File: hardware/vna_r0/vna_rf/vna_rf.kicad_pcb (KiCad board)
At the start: 4 copper layers, 78 x 49 mm, 131 parts, among them J301 RF_Shield_Two_Pieces, J302 RF_Shield_Two_Pieces, J401 CONN_02X10, J402 RF_Shield_Two_Pieces, U201 LMX2594, U202 LTC2630, U203 ADRF5040, U204 LTC2054CS5, U205 MAAM-011100, U301 NC7WZU04, U302 PE42521, U303 MASW-008322-TR1000, U304 PE42521, U401 CONN_SMA_2GND, U402 CONN_SMA_2GND, U403 CONN_SMA, U404 CONN_SMA, U405 CONN_SMA, U406 CONN_SMA_2GND

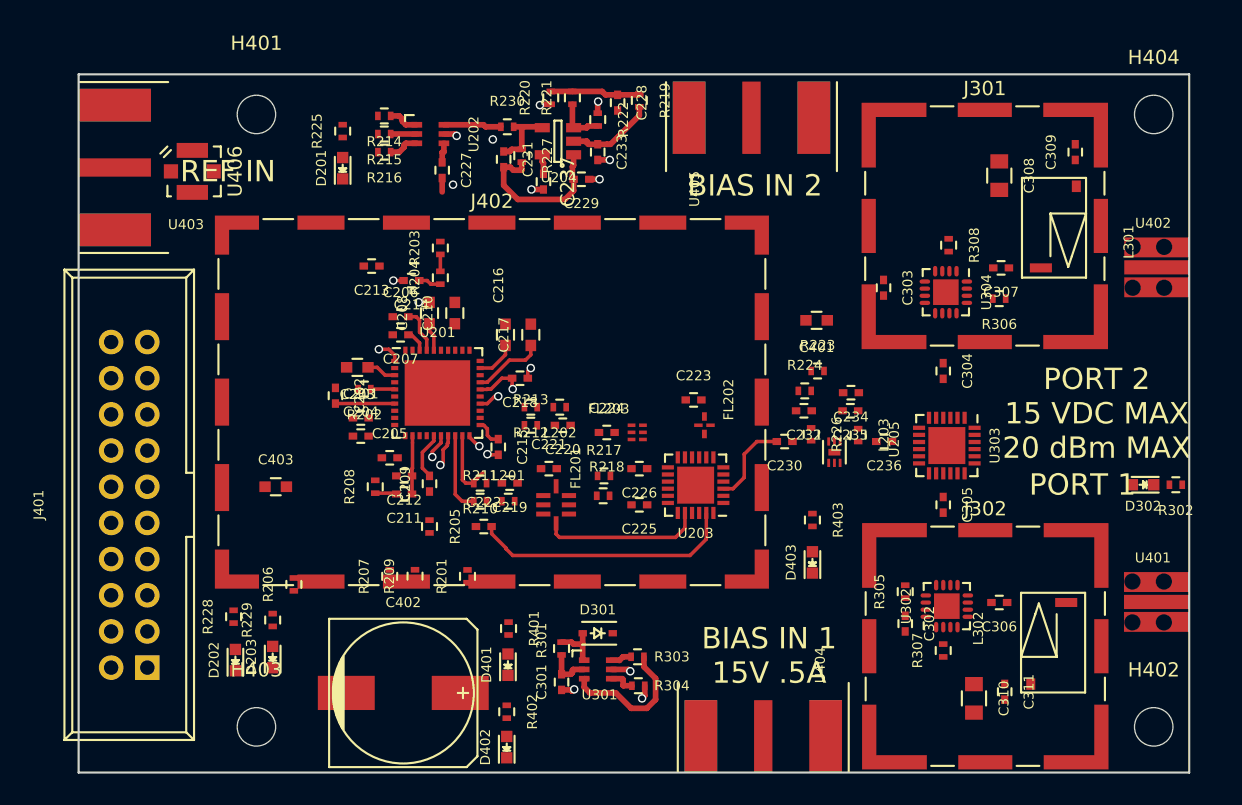
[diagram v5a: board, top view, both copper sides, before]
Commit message: routing vna rf r0
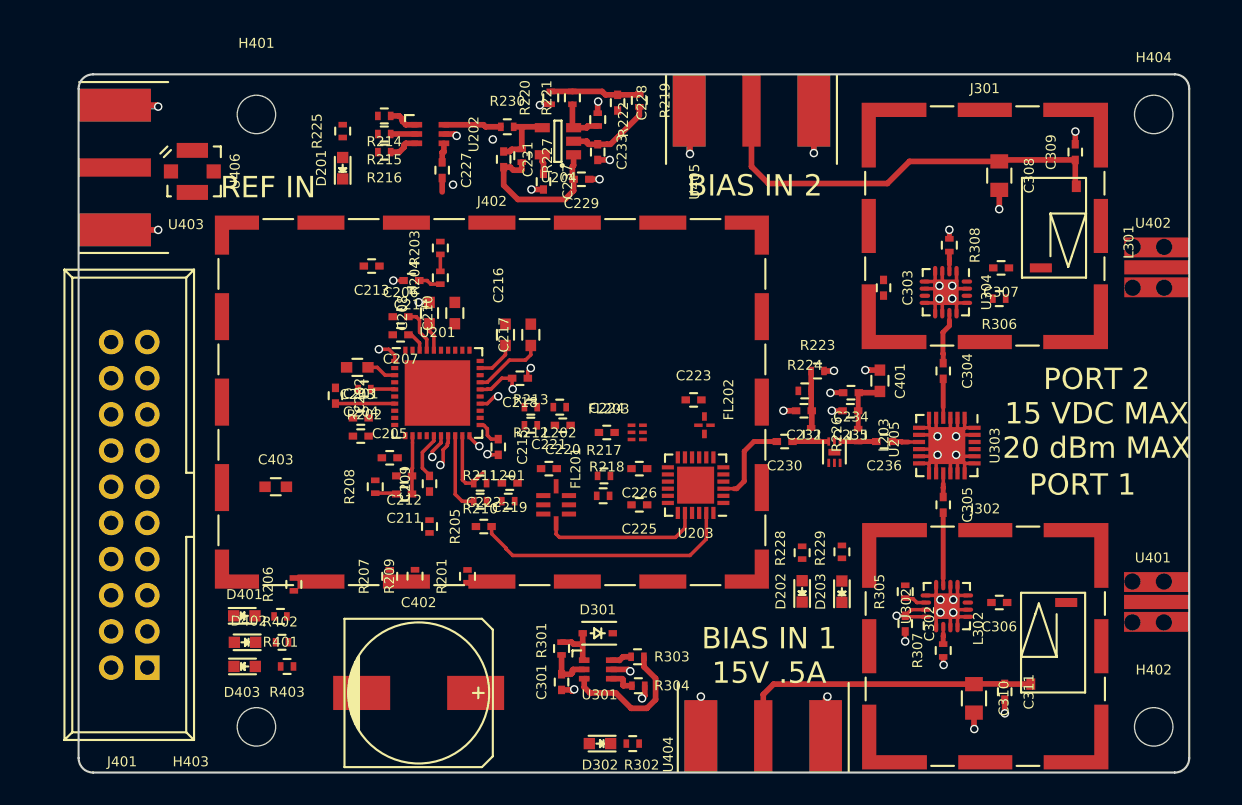
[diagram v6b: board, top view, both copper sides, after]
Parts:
- moved R302 42.2 mm to (214.4, 122.2)
- moved D302 42.2 mm to (212.1, 122.2)
- moved D403 40.5 mm to (187.2, 116.8), turned to 0 degrees
- moved R229 40.3 mm to (229.1, 108.7)
- moved D203 40.2 mm to (229.1, 111.5)
- moved R228 40.2 mm to (226.3, 108.8)
- moved D202 40.1 mm to (226.3, 111.5)
- moved R403 38.3 mm to (190.2, 116.8), turned to 180 degrees
- moved D402 19.8 mm to (187.2, 115.1), turned to 180 degrees
- moved D401 18.8 mm to (187.2, 113.2), turned to 0 degrees
- moved R402 16.5 mm to (189.8, 115.1), turned to 0 degrees
- moved R401 16.0 mm to (189.7, 113.2), turned to 180 degrees
- moved C401 6.15 mm to (231.8, 96.7), turned to 90 degrees
- moved C402 1.08 mm to (199.4, 118.6)
- moved U405 0.51 mm to (222.8, 77.7)
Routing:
- net GND: track 11.4 -> 102.5 mm, vias 12 -> 42
- net /PORT2_BIAS: track 0.00 -> 29.2 mm
- net /PORT1_BIAS: track 0.00 -> 22.0 mm
- net Net-(C305-Pad2): track 0.00 -> 5.09 mm
- net /AMP_5V: track 0.00 -> 4.06 mm
- net Net-(C232-Pad1): track 0.00 -> 4.03 mm
- net Net-(C304-Pad1): track 0.00 -> 3.88 mm
- net +3V3: track 18.8 -> 22.5 mm, vias 1 -> 2
- net Net-(C236-Pad2): track 0.00 -> 2.76 mm
- net Net-(C304-Pad2): track 0.00 -> 2.74 mm
- net Net-(C230-Pad1): track 0.00 -> 2.55 mm
- net /port_switch/RFIN: track 0.00 -> 1.92 mm
- net Net-(C305-Pad1): track 0.00 -> 1.66 mm
- net Net-(R305-Pad1): track 0.00 -> 1.58 mm
- net Net-(R308-Pad2): track 0.00 -> 1.38 mm
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- added copper zone on In2.Cu, net +3V3
- added copper zone on In1.Cu, net GND
- added copper zone on In2.Cu, net GND
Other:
- outline, holes or cut-outs redrawn

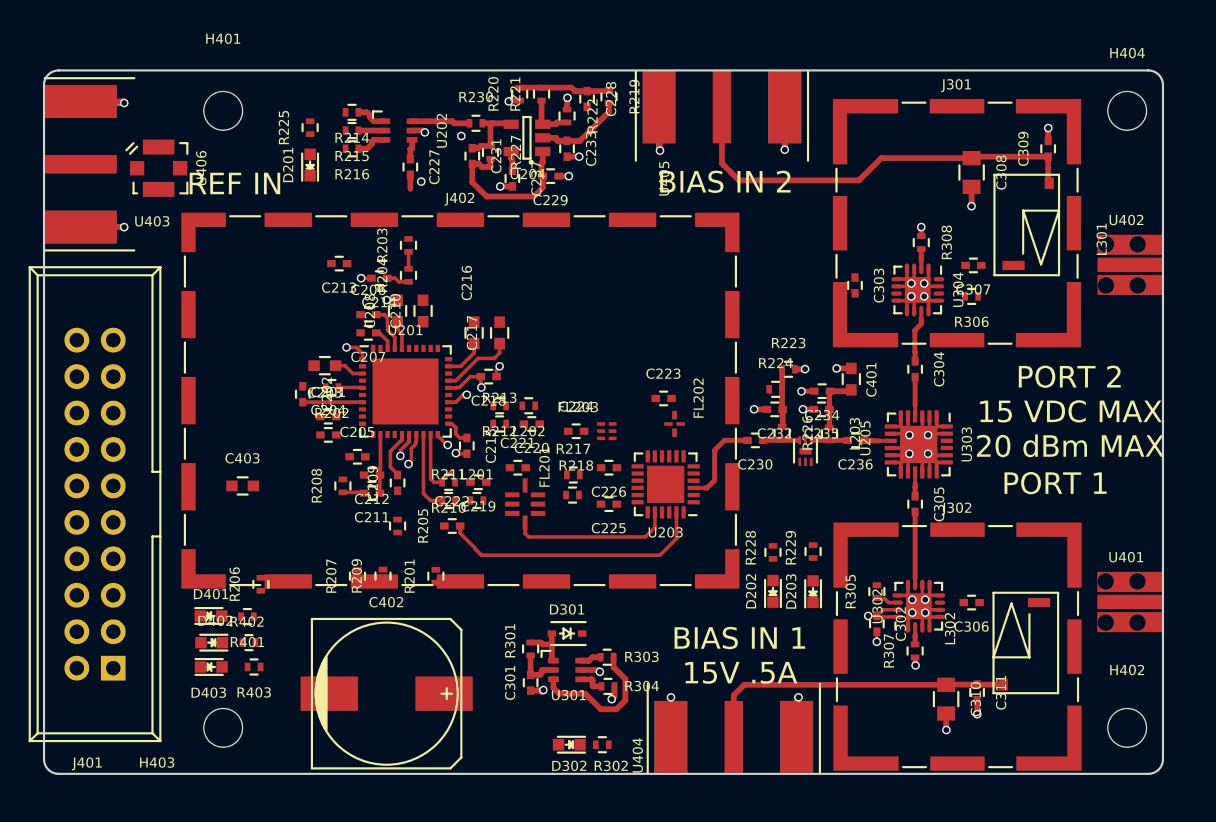
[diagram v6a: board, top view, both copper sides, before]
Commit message: layout of vna r0 rf board
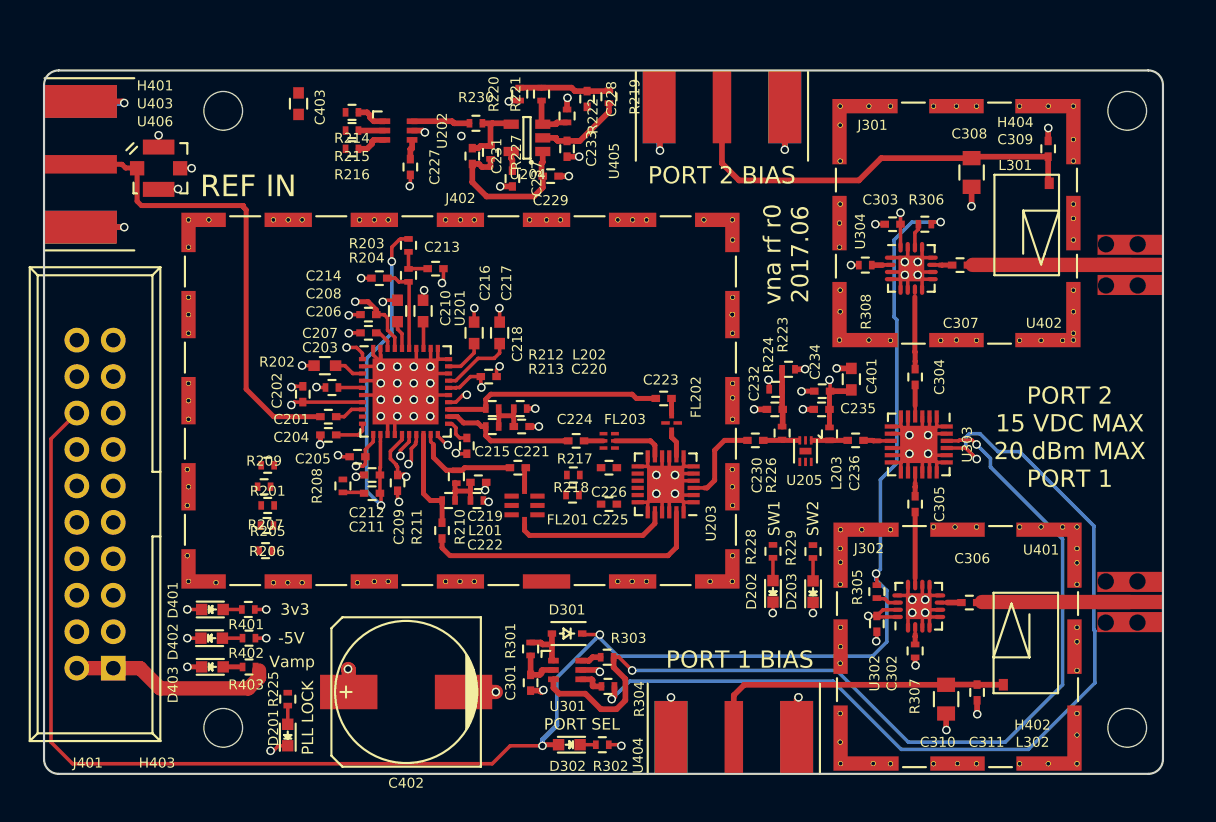
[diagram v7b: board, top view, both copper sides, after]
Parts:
- added REF**: VIA_OSH4LAYER_MIN, vna_footprints:VIA_OSH4LAYER_MIN, F.Cu at (223.5, 105.5)
- added REF** (x2): VIA_OSH4LAYER_MIN, vna_footprints:VIA_OSH4LAYER_MIN, F.Cu at (223.5, 92.2)
- added REF**: VIA_OSH4LAYER_MIN, vna_footprints:VIA_OSH4LAYER_MIN, F.Cu at (233.0, 77.7)
- added REF**: VIA_OSH4LAYER_MIN, vna_footprints:VIA_OSH4LAYER_MIN, F.Cu at (234.5, 77.7)
- added REF**: VIA_OSH4LAYER_MIN, vna_footprints:VIA_OSH4LAYER_MIN, F.Cu at (237.5, 77.7)
- added REF**: VIA_OSH4LAYER_MIN, vna_footprints:VIA_OSH4LAYER_MIN, F.Cu at (239.1, 77.7)
- added REF**: VIA_OSH4LAYER_MIN, vna_footprints:VIA_OSH4LAYER_MIN, F.Cu at (240.5, 77.7)
- added REF**: VIA_OSH4LAYER_MIN, vna_footprints:VIA_OSH4LAYER_MIN, F.Cu at (243.5, 77.7)
- added REF**: VIA_OSH4LAYER_MIN, vna_footprints:VIA_OSH4LAYER_MIN, F.Cu at (245.5, 77.7)
- added REF**: VIA_OSH4LAYER_MIN, vna_footprints:VIA_OSH4LAYER_MIN, F.Cu at (247.2, 77.7)
- added REF**: VIA_OSH4LAYER_MIN, vna_footprints:VIA_OSH4LAYER_MIN, F.Cu at (247.2, 80.0)
- added REF**: VIA_OSH4LAYER_MIN, vna_footprints:VIA_OSH4LAYER_MIN, F.Cu at (247.2, 81.5)
- added REF**: VIA_OSH4LAYER_MIN, vna_footprints:VIA_OSH4LAYER_MIN, F.Cu at (223.5, 87.0)
- added REF**: VIA_OSH4LAYER_MIN, vna_footprints:VIA_OSH4LAYER_MIN, F.Cu at (247.2, 84.5)
- added REF**: VIA_OSH4LAYER_MIN, vna_footprints:VIA_OSH4LAYER_MIN, F.Cu at (247.2, 85.5)
- added REF**: VIA_OSH4LAYER_MIN, vna_footprints:VIA_OSH4LAYER_MIN, F.Cu at (247.2, 87.0)
- added REF**: VIA_OSH4LAYER_MIN, vna_footprints:VIA_OSH4LAYER_MIN, F.Cu at (247.2, 90.5)
- added REF**: VIA_OSH4LAYER_MIN, vna_footprints:VIA_OSH4LAYER_MIN, F.Cu at (247.2, 92.0)
- added REF**: VIA_OSH4LAYER_MIN, vna_footprints:VIA_OSH4LAYER_MIN, F.Cu at (247.2, 93.5)
- added REF**: VIA_OSH4LAYER_MIN, vna_footprints:VIA_OSH4LAYER_MIN, F.Cu at (247.2, 94.0)
- added REF**: VIA_OSH4LAYER_MIN, vna_footprints:VIA_OSH4LAYER_MIN, F.Cu at (246.5, 94.0)
- added REF**: VIA_OSH4LAYER_MIN, vna_footprints:VIA_OSH4LAYER_MIN, F.Cu at (245.0, 94.0)
- added REF**: VIA_OSH4LAYER_MIN, vna_footprints:VIA_OSH4LAYER_MIN, F.Cu at (243.5, 94.0)
- added REF**: VIA_OSH4LAYER_MIN, vna_footprints:VIA_OSH4LAYER_MIN, F.Cu at (223.5, 85.6)
- added REF**: VIA_OSH4LAYER_MIN, vna_footprints:VIA_OSH4LAYER_MIN, F.Cu at (240.5, 94.0)
- added REF**: VIA_OSH4LAYER_MIN, vna_footprints:VIA_OSH4LAYER_MIN, F.Cu at (239.1, 94.0)
- added REF**: VIA_OSH4LAYER_MIN, vna_footprints:VIA_OSH4LAYER_MIN, F.Cu at (238.0, 94.0)
- added REF**: VIA_OSH4LAYER_MIN, vna_footprints:VIA_OSH4LAYER_MIN, F.Cu at (234.5, 94.0)
- added REF**: VIA_OSH4LAYER_MIN, vna_footprints:VIA_OSH4LAYER_MIN, F.Cu at (233.0, 94.0)
- added REF**: VIA_OSH4LAYER_MIN, vna_footprints:VIA_OSH4LAYER_MIN, F.Cu at (230.9, 94.0)
- added REF**: VIA_OSH4LAYER_MIN, vna_footprints:VIA_OSH4LAYER_MIN, F.Cu at (231.0, 92.0)
- added REF**: VIA_OSH4LAYER_MIN, vna_footprints:VIA_OSH4LAYER_MIN, F.Cu at (231.0, 90.5)
- added REF**: VIA_OSH4LAYER_MIN, vna_footprints:VIA_OSH4LAYER_MIN, F.Cu at (221.5, 85.6)
- added REF**: VIA_OSH4LAYER_MIN, vna_footprints:VIA_OSH4LAYER_MIN, F.Cu at (217.5, 85.6)
- added REF**: VIA_OSH4LAYER_MIN, vna_footprints:VIA_OSH4LAYER_MIN, F.Cu at (215.5, 85.6)
- added REF**: VIA_OSH4LAYER_MIN, vna_footprints:VIA_OSH4LAYER_MIN, F.Cu at (216.5, 85.6)
- added REF**: VIA_OSH4LAYER_MIN, vna_footprints:VIA_OSH4LAYER_MIN, F.Cu at (211.5, 85.6)
- added REF**: VIA_OSH4LAYER_MIN, vna_footprints:VIA_OSH4LAYER_MIN, F.Cu at (209.3, 85.6)
- added REF**: VIA_OSH4LAYER_MIN, vna_footprints:VIA_OSH4LAYER_MIN, F.Cu at (210.5, 85.6)
- added REF**: VIA_OSH4LAYER_MIN, vna_footprints:VIA_OSH4LAYER_MIN, F.Cu at (223.5, 103.0)
- added REF**: VIA_OSH4LAYER_MIN, vna_footprints:VIA_OSH4LAYER_MIN, F.Cu at (205.5, 85.6)
- added REF**: VIA_OSH4LAYER_MIN, vna_footprints:VIA_OSH4LAYER_MIN, F.Cu at (203.5, 85.6)
- added REF**: VIA_OSH4LAYER_MIN, vna_footprints:VIA_OSH4LAYER_MIN, F.Cu at (204.5, 85.6)
- added REF**: VIA_OSH4LAYER_MIN, vna_footprints:VIA_OSH4LAYER_MIN, F.Cu at (199.5, 85.6)
- added REF**: VIA_OSH4LAYER_MIN, vna_footprints:VIA_OSH4LAYER_MIN, F.Cu at (198.5, 85.6)
- added REF**: VIA_OSH4LAYER_MIN, vna_footprints:VIA_OSH4LAYER_MIN, F.Cu at (197.5, 85.6)
- added REF**: VIA_OSH4LAYER_MIN, vna_footprints:VIA_OSH4LAYER_MIN, F.Cu at (193.5, 85.6)
- added REF**: VIA_OSH4LAYER_MIN, vna_footprints:VIA_OSH4LAYER_MIN, F.Cu at (192.5, 85.6)
- added REF**: VIA_OSH4LAYER_MIN, vna_footprints:VIA_OSH4LAYER_MIN, F.Cu at (191.5, 85.6)
- added REF**: VIA_OSH4LAYER_MIN, vna_footprints:VIA_OSH4LAYER_MIN, F.Cu at (187.0, 85.6)
- added REF**: VIA_OSH4LAYER_MIN, vna_footprints:VIA_OSH4LAYER_MIN, F.Cu at (223.5, 104.2)
- added REF**: VIA_OSH4LAYER_MIN, vna_footprints:VIA_OSH4LAYER_MIN, F.Cu at (185.6, 85.6)
- added REF**: VIA_OSH4LAYER_MIN, vna_footprints:VIA_OSH4LAYER_MIN, F.Cu at (185.6, 87.5)
- added REF**: VIA_OSH4LAYER_MIN, vna_footprints:VIA_OSH4LAYER_MIN, F.Cu at (185.6, 91.0)
- added REF**: VIA_OSH4LAYER_MIN, vna_footprints:VIA_OSH4LAYER_MIN, F.Cu at (185.6, 93.5)
- added REF**: VIA_OSH4LAYER_MIN, vna_footprints:VIA_OSH4LAYER_MIN, F.Cu at (185.6, 92.2)
- added REF**: VIA_OSH4LAYER_MIN, vna_footprints:VIA_OSH4LAYER_MIN, F.Cu at (185.6, 97.0)
- added REF**: VIA_OSH4LAYER_MIN, vna_footprints:VIA_OSH4LAYER_MIN, F.Cu at (185.6, 99.5)
- added REF**: VIA_OSH4LAYER_MIN, vna_footprints:VIA_OSH4LAYER_MIN, F.Cu at (185.6, 98.2)
- added REF**: VIA_OSH4LAYER_MIN, vna_footprints:VIA_OSH4LAYER_MIN, F.Cu at (185.5, 103.0)
- added REF**: VIA_OSH4LAYER_MIN, vna_footprints:VIA_OSH4LAYER_MIN, F.Cu at (185.6, 104.2)
- added REF**: VIA_OSH4LAYER_MIN, vna_footprints:VIA_OSH4LAYER_MIN, F.Cu at (223.5, 99.5)
- added REF**: VIA_OSH4LAYER_MIN, vna_footprints:VIA_OSH4LAYER_MIN, F.Cu at (185.5, 105.5)
- added REF**: VIA_OSH4LAYER_MIN, vna_footprints:VIA_OSH4LAYER_MIN, F.Cu at (185.5, 109.0)
- added REF**: VIA_OSH4LAYER_MIN, vna_footprints:VIA_OSH4LAYER_MIN, F.Cu at (185.6, 110.8)
- added REF**: VIA_OSH4LAYER_MIN, vna_footprints:VIA_OSH4LAYER_MIN, F.Cu at (187.5, 110.9)
- added REF**: VIA_OSH4LAYER_MIN, vna_footprints:VIA_OSH4LAYER_MIN, F.Cu at (191.5, 110.9)
- added REF**: VIA_OSH4LAYER_MIN, vna_footprints:VIA_OSH4LAYER_MIN, F.Cu at (192.5, 110.9)
- added REF**: VIA_OSH4LAYER_MIN, vna_footprints:VIA_OSH4LAYER_MIN, F.Cu at (193.5, 110.9)
- added REF**: VIA_OSH4LAYER_MIN, vna_footprints:VIA_OSH4LAYER_MIN, F.Cu at (197.4, 110.9)
- added REF**: VIA_OSH4LAYER_MIN, vna_footprints:VIA_OSH4LAYER_MIN, F.Cu at (198.5, 110.8)
- added REF**: VIA_OSH4LAYER_MIN, vna_footprints:VIA_OSH4LAYER_MIN, F.Cu at (199.5, 110.8)
- added REF**: VIA_OSH4LAYER_MIN, vna_footprints:VIA_OSH4LAYER_MIN, F.Cu at (223.5, 97.0)
- added REF**: VIA_OSH4LAYER_MIN, vna_footprints:VIA_OSH4LAYER_MIN, F.Cu at (203.5, 110.8)
- added REF**: VIA_OSH4LAYER_MIN, vna_footprints:VIA_OSH4LAYER_MIN, F.Cu at (204.5, 110.8)
- added REF**: VIA_OSH4LAYER_MIN, vna_footprints:VIA_OSH4LAYER_MIN, F.Cu at (205.5, 110.8)
- added REF**: VIA_OSH4LAYER_MIN, vna_footprints:VIA_OSH4LAYER_MIN, F.Cu at (215.5, 110.8)
- added REF**: VIA_OSH4LAYER_MIN, vna_footprints:VIA_OSH4LAYER_MIN, F.Cu at (216.5, 110.8)
- added REF**: VIA_OSH4LAYER_MIN, vna_footprints:VIA_OSH4LAYER_MIN, F.Cu at (217.5, 110.8)
- added REF**: VIA_OSH4LAYER_MIN, vna_footprints:VIA_OSH4LAYER_MIN, F.Cu at (221.9, 110.8)
- added REF**: VIA_OSH4LAYER_MIN, vna_footprints:VIA_OSH4LAYER_MIN, F.Cu at (223.5, 109.0)
- added REF**: VIA_OSH4LAYER_MIN, vna_footprints:VIA_OSH4LAYER_MIN, F.Cu at (223.5, 110.8)
- added REF**: VIA_OSH4LAYER_MIN, vna_footprints:VIA_OSH4LAYER_MIN, F.Cu at (234.5, 107.2)
- added REF**: VIA_OSH4LAYER_MIN, vna_footprints:VIA_OSH4LAYER_MIN, F.Cu at (223.5, 98.0)
- added REF**: VIA_OSH4LAYER_MIN, vna_footprints:VIA_OSH4LAYER_MIN, F.Cu at (232.5, 107.2)
- added REF**: VIA_OSH4LAYER_MIN, vna_footprints:VIA_OSH4LAYER_MIN, F.Cu at (231.0, 107.2)
- added REF**: VIA_OSH4LAYER_MIN, vna_footprints:VIA_OSH4LAYER_MIN, F.Cu at (231.0, 108.5)
- added REF**: VIA_OSH4LAYER_MIN, vna_footprints:VIA_OSH4LAYER_MIN, F.Cu at (231.0, 109.5)
- added REF**: VIA_OSH4LAYER_MIN, vna_footprints:VIA_OSH4LAYER_MIN, F.Cu at (231.0, 111.0)
- added REF**: VIA_OSH4LAYER_MIN, vna_footprints:VIA_OSH4LAYER_MIN, F.Cu at (231.0, 114.0)
- added REF**: VIA_OSH4LAYER_MIN, vna_footprints:VIA_OSH4LAYER_MIN, F.Cu at (231.0, 115.3)
- added REF**: VIA_OSH4LAYER_MIN, vna_footprints:VIA_OSH4LAYER_MIN, F.Cu at (231.0, 116.5)
- added REF**: VIA_OSH4LAYER_MIN, vna_footprints:VIA_OSH4LAYER_MIN, F.Cu at (231.0, 120.0)
- added REF**: VIA_OSH4LAYER_MIN, vna_footprints:VIA_OSH4LAYER_MIN, F.Cu at (231.0, 122.0)
- added REF**: VIA_OSH4LAYER_MIN, vna_footprints:VIA_OSH4LAYER_MIN, F.Cu at (223.5, 93.5)
- added REF**: VIA_OSH4LAYER_MIN, vna_footprints:VIA_OSH4LAYER_MIN, F.Cu at (231.0, 123.5)
- added REF**: VIA_OSH4LAYER_MIN, vna_footprints:VIA_OSH4LAYER_MIN, F.Cu at (233.3, 123.5)
- added REF**: VIA_OSH4LAYER_MIN, vna_footprints:VIA_OSH4LAYER_MIN, F.Cu at (234.5, 123.5)
- added REF**: VIA_OSH4LAYER_MIN, vna_footprints:VIA_OSH4LAYER_MIN, F.Cu at (237.5, 123.5)
- added REF**: VIA_OSH4LAYER_MIN, vna_footprints:VIA_OSH4LAYER_MIN, F.Cu at (239.2, 123.5)
- added REF**: VIA_OSH4LAYER_MIN, vna_footprints:VIA_OSH4LAYER_MIN, F.Cu at (240.5, 123.5)
- added REF**: VIA_OSH4LAYER_MIN, vna_footprints:VIA_OSH4LAYER_MIN, F.Cu at (243.5, 123.5)
- added REF**: VIA_OSH4LAYER_MIN, vna_footprints:VIA_OSH4LAYER_MIN, F.Cu at (245.5, 123.5)
- added REF**: VIA_OSH4LAYER_MIN, vna_footprints:VIA_OSH4LAYER_MIN, F.Cu at (247.5, 123.5)
- added REF**: VIA_OSH4LAYER_MIN, vna_footprints:VIA_OSH4LAYER_MIN, F.Cu at (247.5, 121.5)
- added REF**: VIA_OSH4LAYER_MIN, vna_footprints:VIA_OSH4LAYER_MIN, F.Cu at (223.5, 91.0)
- added REF**: VIA_OSH4LAYER_MIN, vna_footprints:VIA_OSH4LAYER_MIN, F.Cu at (247.5, 120.0)
- added REF**: VIA_OSH4LAYER_MIN, vna_footprints:VIA_OSH4LAYER_MIN, F.Cu at (247.5, 117.0)
- added REF**: VIA_OSH4LAYER_MIN, vna_footprints:VIA_OSH4LAYER_MIN, F.Cu at (247.5, 115.0)
- added REF**: VIA_OSH4LAYER_MIN, vna_footprints:VIA_OSH4LAYER_MIN, F.Cu at (247.5, 114.0)
- added REF**: VIA_OSH4LAYER_MIN, vna_footprints:VIA_OSH4LAYER_MIN, F.Cu at (247.5, 111.0)
- added REF**: VIA_OSH4LAYER_MIN, vna_footprints:VIA_OSH4LAYER_MIN, F.Cu at (247.5, 109.5)
- added REF**: VIA_OSH4LAYER_MIN, vna_footprints:VIA_OSH4LAYER_MIN, F.Cu at (247.5, 108.5)
- added REF**: VIA_OSH4LAYER_MIN, vna_footprints:VIA_OSH4LAYER_MIN, F.Cu at (247.5, 107.0)
- added REF**: VIA_OSH4LAYER_MIN, vna_footprints:VIA_OSH4LAYER_MIN, F.Cu at (246.5, 107.0)
- added REF**: VIA_OSH4LAYER_MIN, vna_footprints:VIA_OSH4LAYER_MIN, F.Cu at (245.0, 107.0)
- added REF**: VIA_OSH4LAYER_MIN, vna_footprints:VIA_OSH4LAYER_MIN, F.Cu at (243.5, 107.0)
- added REF**: VIA_OSH4LAYER_MIN, vna_footprints:VIA_OSH4LAYER_MIN, F.Cu at (240.5, 107.0)
- added REF**: VIA_OSH4LAYER_MIN, vna_footprints:VIA_OSH4LAYER_MIN, F.Cu at (239.0, 107.0)
- added REF**: VIA_OSH4LAYER_MIN, vna_footprints:VIA_OSH4LAYER_MIN, F.Cu at (237.5, 107.0)
- added REF**: VIA_OSH4LAYER_MIN, vna_footprints:VIA_OSH4LAYER_MIN, F.Cu at (230.9, 87.5)
- added REF**: VIA_OSH4LAYER_MIN, vna_footprints:VIA_OSH4LAYER_MIN, F.Cu at (230.9, 85.8)
- added REF**: VIA_OSH4LAYER_MIN, vna_footprints:VIA_OSH4LAYER_MIN, F.Cu at (231.0, 84.5)
- added REF**: VIA_OSH4LAYER_MIN, vna_footprints:VIA_OSH4LAYER_MIN, F.Cu at (231.0, 81.5)
- added REF**: VIA_OSH4LAYER_MIN, vna_footprints:VIA_OSH4LAYER_MIN, F.Cu at (231.0, 79.0)
- added REF**: VIA_OSH4LAYER_MIN, vna_footprints:VIA_OSH4LAYER_MIN, F.Cu at (231.0, 77.7)
- moved R225 39.9 mm to (192.5, 119.0)
- moved D201 39.8 mm to (192.5, 121.5)
- moved C403 26.9 mm to (193.2, 77.5), turned to 270 degrees
- moved R201 14.0 mm to (191.1, 102.7), turned to 180 degrees
- moved R209 10.4 mm to (190.8, 104.2), turned to 0 degrees
- moved R205 9.16 mm to (191.1, 105.5), turned to 180 degrees
- moved C213 6.72 mm to (202.8, 89.0), turned to 0 degrees
- moved R207 6.65 mm to (190.9, 108.7), turned to 0 degrees
- moved R306 5.99 mm to (236.9, 85.9), turned to 0 degrees
- moved C303 5.01 mm to (234.7, 85.9), turned to 180 degrees
- moved R308 4.20 mm to (232.8, 88.8), turned to 0 degrees
- moved R206 4.12 mm to (191.1, 106.9), turned to 180 degrees
- moved U304 1.57 mm to (236.0, 89.0), turned to 0 degrees
- moved C402 1.37 mm to (200.8, 118.5), turned to 180 degrees
- moved C307 0.93 mm to (239.3, 88.8)
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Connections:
- U304 pad 11: Net-(C304-Pad1) -> Net-(C307-Pad2)
- U304 pad 7: Net-(C307-Pad2) -> Net-(C304-Pad1)
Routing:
- net /conn_power/PORT_SEL: track 0.00 -> 126.5 mm, vias 0 -> 4
- net GND: track 102.5 -> 168.0 mm, vias 42 -> 90
- net /port_switch/SW_V1: track 0.97 -> 65.9 mm, vias 1 -> 2
- net /port_switch/SW_V2: track 10.0 -> 66.9 mm, vias 0 -> 2
- net /conn_power/SYNTH_REF: track 0.00 -> 32.7 mm
- net /rf_synth/CPOUT: track 4.11 -> 25.5 mm, vias 0 -> 2
- net /rf_synth/RFOUTAP: track 0.00 -> 15.4 mm
- net /AMP_5V: track 4.06 -> 19.3 mm, vias 0 -> 1
- net /conn_power/PORT1: track 0.05 -> 15.0 mm
- net /conn_power/PORT2: track 0.00 -> 14.2 mm
- net +3V3: track 22.5 -> 35.0 mm, vias 2 -> 11
- net /rf_synth/RFOUTAM: track 0.00 -> 9.42 mm
- net Net-(C214-Pad1): track 1.59 -> 6.25 mm
- net /rf_synth/RF_3: track 0.00 -> 3.69 mm
- net Net-(C219-Pad2): track 0.00 -> 3.63 mm
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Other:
- net class Default: clearance 0.2 -> 0.126
- rule trace_clearance: 0.2 -> 0.126
- board text added: "-5V"
- board text added: "3v3"
- board text added: "PLL LOCK"
- board text added: "PORT 1 BIAS"
- board text added: "PORT 2 15 VDC MAX 20 dBm MAX PORT 1"
- board text added: "PORT 2 BIAS"
- board text added: "PORT SEL"
- board text added: "SW1"
- board text added: "SW2"
- board text added: "Vamp"
- board text added: "vna rf r0 2017.06"
- board text removed: "BIAS IN 1 15V .5A"
- board text removed: "BIAS IN 2"
- board text removed: "PORT 1"
- board text removed: "PORT 2 15 VDC MAX 20 dBm MAX"
